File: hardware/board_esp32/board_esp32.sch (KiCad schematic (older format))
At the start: 91 parts

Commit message: removes MPPT IC and adds battery load switch
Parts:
- removed C?: 1uF, symbol Device:C_Small
- removed C? (x2): C_Small, symbol Device:C_Small
- removed D?: MBRS340, symbol Device:D_Schottky_Small
- removed D? (x2): STPS2L40U, symbol Device:D_Schottky_Small
- removed D? (x2): TPD1E10B06, Diode_SMD:D_0402_1005Metric, symbol Device:D_TVS
- removed J?: Conn_01x03, symbol Connector_Generic:Conn_01x03
- removed JP?: SolderJumper_2_Open, symbol Jumper:SolderJumper_2_Open
- removed L?: 22uH, symbol Device:L_Small
- removed R? (x4): 1K, symbol Device:R_Small
- removed R? (x2): NC, symbol Device:R_Small
- removed R? (x3): R_Small, symbol Device:R_Small
- removed R?: 0, symbol Device:R_Small
- removed TH?: NC, symbol Device:Thermistor_NTC
- removed U?: LT3652EMSE, Package_SO:MSOP-12-1EP_3x4mm_P0.65mm_EP1.65x2.85mm, symbol Battery_Management:LT3652EMSE
- added C?: 1nF, symbol Device:C_Small
- added J?: Micro_SD_Card_Det_Hirose_DM3AT, symbol Connector:Micro_SD_Card_Det_Hirose_DM3AT
- added J?: Conn_01x02, symbol Connector_Generic:Conn_01x02
- added JP? (x3): SolderJumper_2_Bridged, symbol Jumper:SolderJumper_2_Bridged
- added Q? (x2): AO3401, symbol Device:Q_PMOS_GDS
- added Q?: AO3400, symbol Device:Q_NMOS_GDS
- added R? (x2): 1K, symbol Device:R_Small
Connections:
- net labels removed: ~CHRG, ~FAULT
- wire segments 302 -> 248
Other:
- note added: "BATTERY INPUT 0-17V"
- note added: "BATTERY POWERS WHEN USB NOT CONNECTED"

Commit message: updates pin routing on ESP32
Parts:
- removed C?: 1nF, symbol Device:C_Small
- removed R? (x2): NC, symbol Device:R_Small
- removed R?: 10K, symbol Device:R_Small
- removed SW?: SW_Push, symbol symbols:SW_Push
- removed U?: FT230XS, Package_SO:SSOP-16_3.9x4.9mm_P0.635mm, symbol symbols:FT230XS
- added C? (x2): NC, symbol Device:C_Small
- added D?: BLUE, symbol Device:LED_Small
- added JP? (x15): SolderJumper_2_Bridged, symbol Jumper:SolderJumper_2_Bridged
- added R?: 10K, symbol Device:R_Small
- added U?: FT231XS, Package_SO:SSOP-20_3.9x8.7mm_P0.635mm, symbol symbols:FT231XS
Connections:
- net labels added: ESP_LED, FT_DCD, FT_DSR, FT_DTR, FT_RI, SD_CLK, SD_CMD, SD_DAT0, SD_DAT1, SD_DAT2, SD_DAT3, SD_DET_A, SD_DET_B
- net labels removed: LED0, LED1, SW_INPUT
- wire segments 248 -> 279
- no-connect marks 11 -> 8
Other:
- moved on the sheet: C?, D?, J?, JP?, R?, TP?

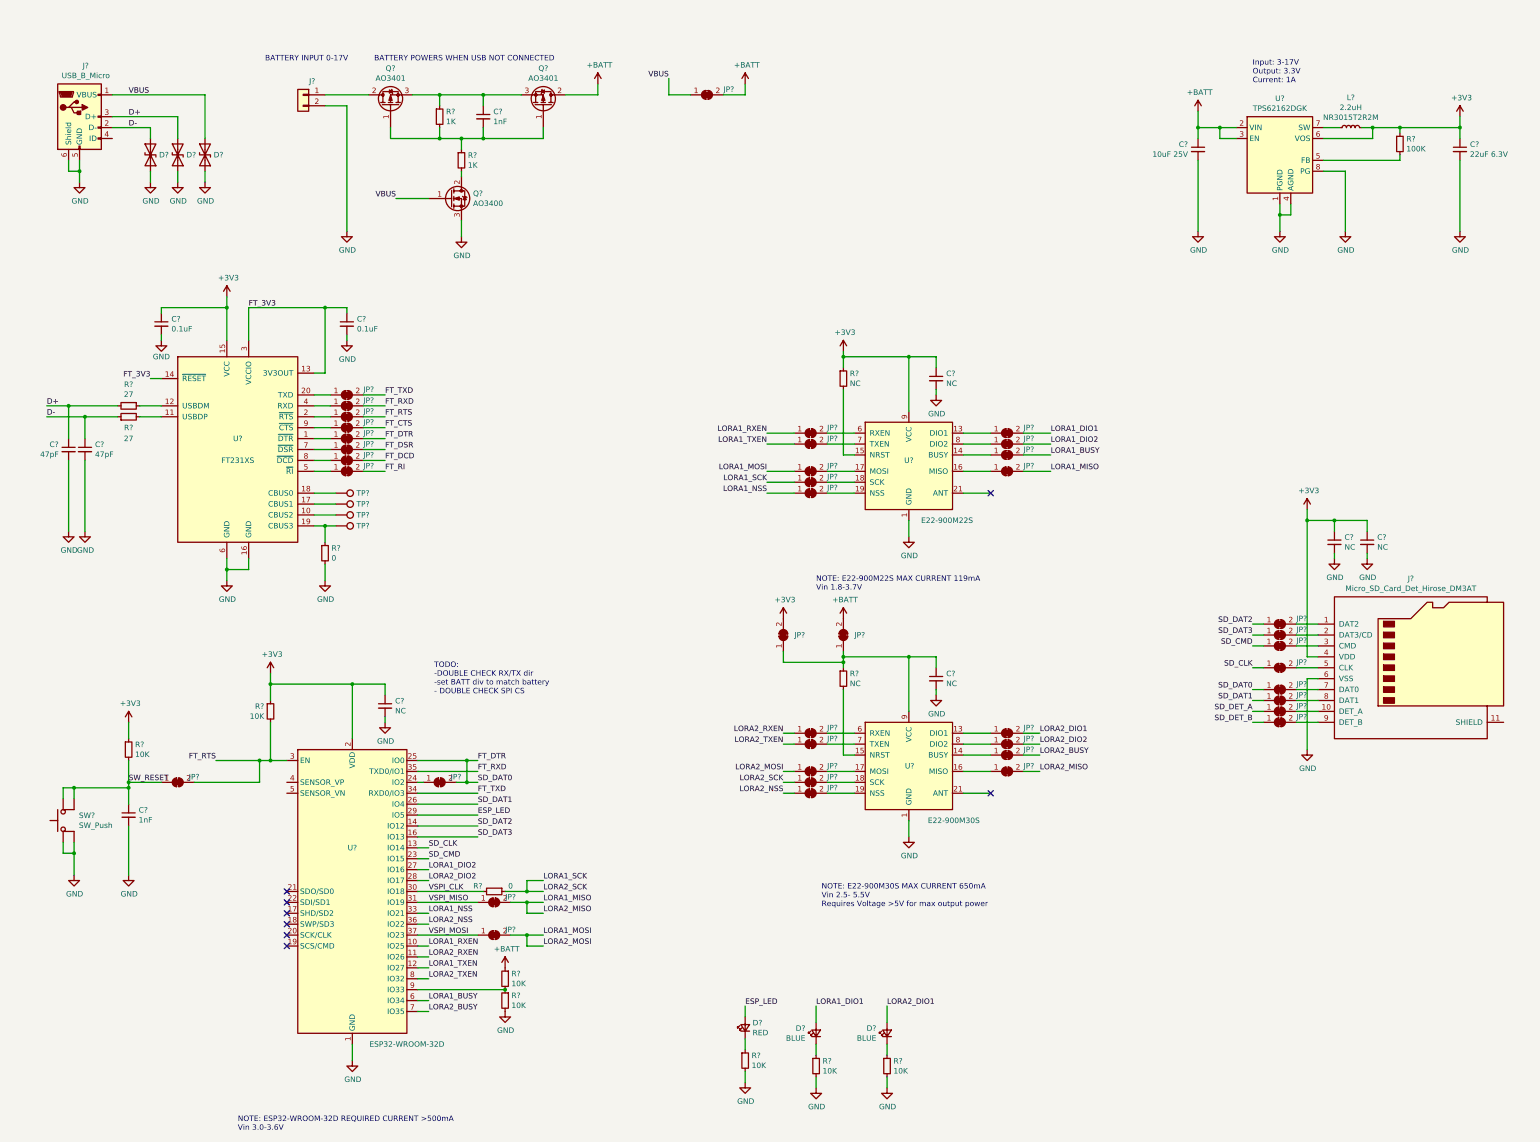
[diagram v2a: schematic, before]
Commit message: adds all footprints and starts work on routing out board ESP32
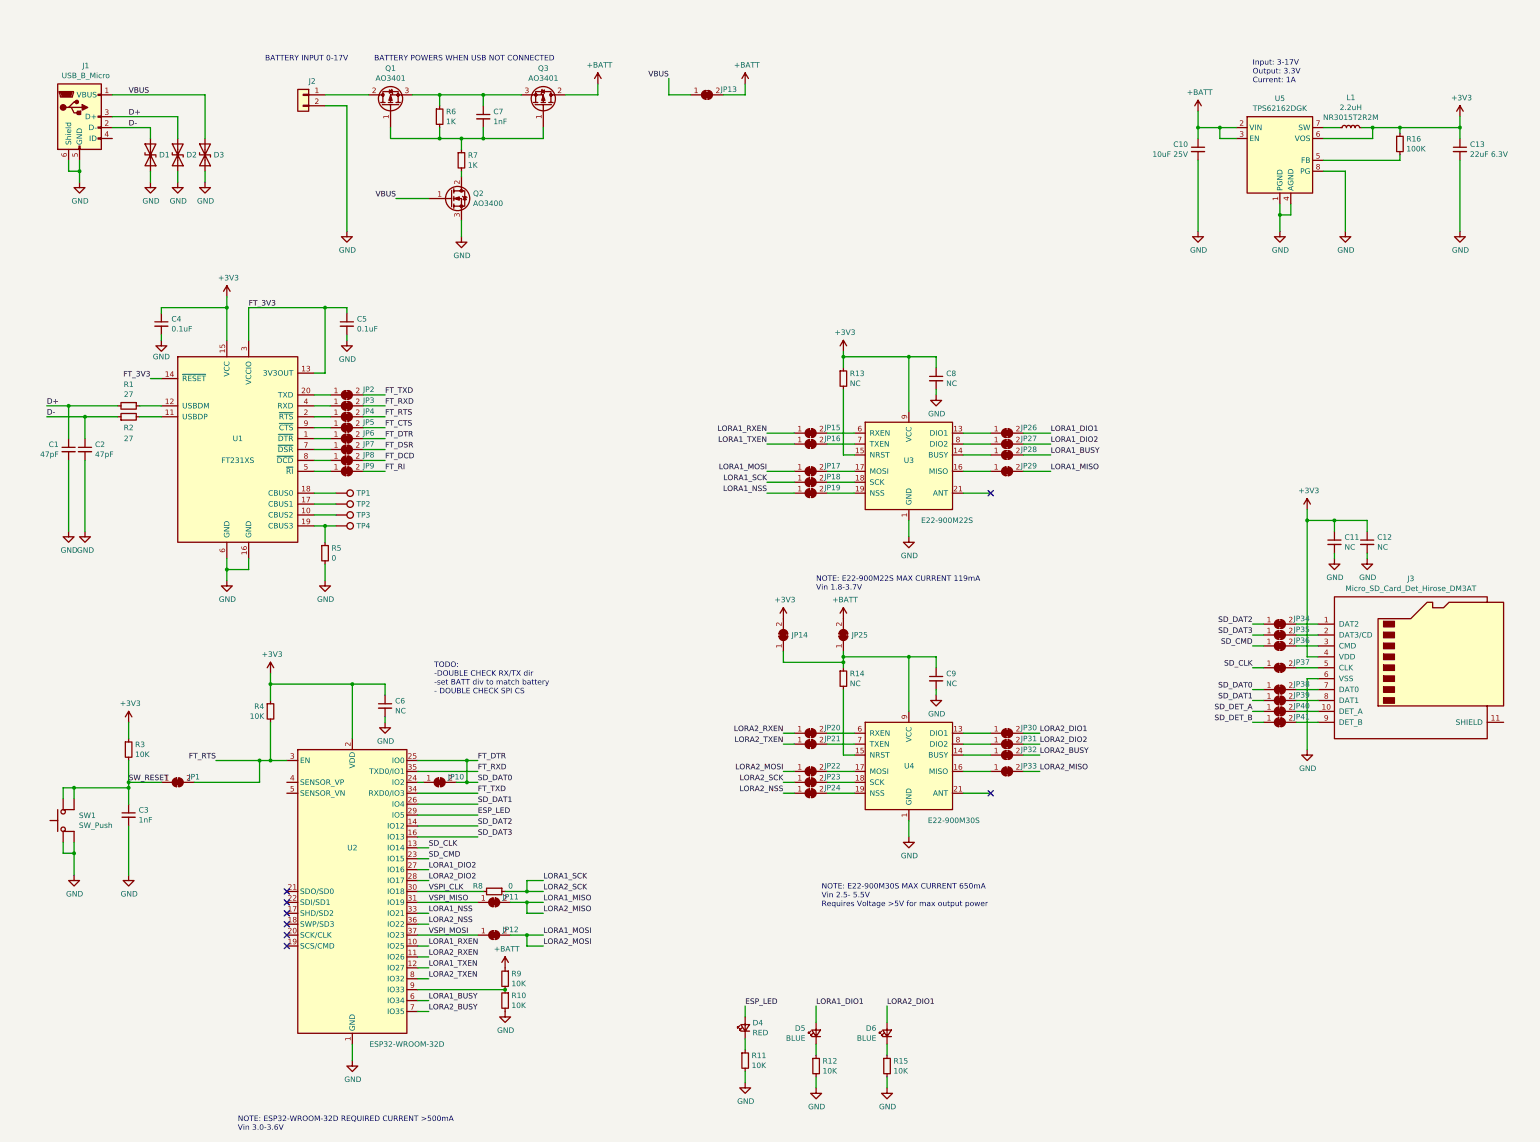
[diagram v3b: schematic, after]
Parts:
- C1, C12, C2, C3, C4, C5, C6, C7, C8, C9: renamed from C?; footprint (none) -> Capacitor_SMD:C_0402_1005Metric
- C10, C11, C13: renamed from C?; footprint (none) -> Capacitor_SMD:C_0805_2012Metric
- D4, D5, D6: renamed from D?; footprint (none) -> LED_SMD:LED_0603_1608Metric
- J1: renamed from J?; footprint (none) -> Connector_USB:USB_Micro-B_GCT_USB3076-30-A
- J2: renamed from J?; footprint (none) -> Connector_PinHeader_2.54mm:PinHeader_1x02_P2.54mm_Vertical
- J3: renamed from J?; footprint (none) -> Connector_Card:microSD_HC_Hirose_DM3D-SF
- JP1, JP10, JP11, JP12, JP13, JP14, JP15, JP16, JP17, JP18, JP19, JP2, JP20, JP21, JP22, JP23, JP24, JP25, JP26, JP27, JP28, JP29, JP3, JP30, JP31, JP32, JP33, JP34, JP35, JP36, JP37, JP38, JP39, JP4, JP40, JP41, JP5, JP6, JP7, JP8, JP9: renamed from JP?; footprint (none) -> Jumper:SolderJumper-2_P1.3mm_Bridged_RoundedPad1.0x1.5mm
- L1: renamed from L?; footprint (none) -> Inductor_SMD:L_Taiyo-Yuden_NR-30xx_HandSoldering
- Q1, Q2, Q3: renamed from Q?; footprint (none) -> Package_TO_SOT_SMD:SOT-23
- R1, R10, R11, R12, R13, R14, R15, R16, R2, R3, R4, R5, R6, R7, R8, R9: renamed from R?; footprint (none) -> Resistor_SMD:R_0402_1005Metric
- SW1: renamed from SW?; footprint (none) -> Button_Switch_SMD:SW_Push_1P1T-SH_NO_CK_KMR2xxG
- TP1, TP2, TP3, TP4: renamed from TP?; footprint (none) -> TestPoint:TestPoint_Pad_1.5x1.5mm
- U3: renamed from U?; footprint (none) -> parts:E22_900T22S
- U4: renamed from U?; footprint (none) -> parts:E22-900M30S
- gave numbers to parts that had none: 6

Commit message: adds changelog and pcb components are organised
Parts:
- removed C11: NC, Capacitor_SMD:C_0805_2012Metric, symbol Device:C_Small
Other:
- note added: "90 Ohm Diff Impedance"
- moved on the sheet: C12
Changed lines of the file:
@@
-	0    -1   -1   0
-$EndComp
-$Comp
-L Jumper:SolderJumper_2_Bridged JP14
-U 1 1 5DD3DBB8
-P 7700 6000
-F 0 "JP14" V 7700 5850 50  0000 C CNN
-F 1 "SolderJumper_2_Bridged" H 7700 6114 50  0001 C CNN
-F 2 "Jumper:SolderJumper-2_P1.3mm_Bridged_RoundedPad1.0x1.5mm" H 7700 6000 50  0001 C CNN
-F 3 "~" H 7700 6000 50  0001 C CNN
-	1    7700 6000
 	0    -1   -1   0
 $EndComp
@@
 $EndComp
 $Comp
-L Device:C_Small C11
-U 1 1 5DD91FE7
-P 12750 5150
-F 0 "C11" H 12842 5196 50  0000 L CNN
-F 1 "NC" H 12842 5105 50  0000 L CNN
-F 2 "Capacitor_SMD:C_0805_2012Metric" H 12750 5150 50  0001 C CNN
-F 3 "~" H 12750 5150 50  0001 C CNN
-	1    12750 5150
-	1    0    0    -1
-$EndComp
-$Comp
 L Device:C_Small C12
 U 1 1 5DD9356A
-P 13050 5150
-F 0 "C12" H 13142 5196 50  0000 L CNN
-F 1 "NC" H 13142 5105 50  0000 L CNN
-F 2 "Capacitor_SMD:C_0402_1005Metric" H 13050 5150 50  0001 C CNN
-F 3 "~" H 13050 5150 50  0001 C CNN
-	1    13050 5150
-	1    0    0    -1
-$EndComp
-$Comp
-L power:GND #PWR0140
-U 1 1 5DD93A75
-P 12750 5300
-F 0 "#PWR0140" H 12750 5050 50  0001 C CNN
-F 1 "GND" H 12755 5127 50  0000 C CNN
-F 2 "" H 12750 5300 50  0001 C CNN
-F 3 "" H 12750 5300 50  0001 C CNN
-	1    12750 5300
+P 12800 5150
+F 0 "C12" H 12892 5196 50  0000 L CNN
+F 1 "NC" H 12892 5105 50  0000 L CNN
+F 2 "Capacitor_SMD:C_0402_1005Metric" H 12800 5150 50  0001 C CNN
+F 3 "~" H 12800 5150 50  0001 C CNN
+	1    12800 5150
 	1    0    0    -1
 $EndComp
@@
 L power:GND #PWR0141
 U 1 1 5DD94190
-P 13050 5300
-F 0 "#PWR0141" H 13050 5050 50  0001 C CNN
-F 1 "GND" H 13055 5127 50  0000 C CNN
-F 2 "" H 13050 5300 50  0001 C CNN
-F 3 "" H 13050 5300 50  0001 C CNN
-	1    13050 5300
-	1    0    0    -1
-$EndComp
-Wire Wire Line
-	12500 4950 12750 4950
-Wire Wire Line
-	13050 4950 13050 5050
+P 12800 5300
+F 0 "#PWR0141" H 12800 5050 50  0001 C CNN
+F 1 "GND" H 12805 5127 50  0000 C CNN
+F 2 "" H 12800 5300 50  0001 C CNN
+F 3 "" H 12800 5300 50  0001 C CNN
+	1    12800 5300
+	1    0    0    -1
+$EndComp
+Wire Wire Line
+	12800 4950 12800 5050
 Connection ~ 12500 4950
 Wire Wire Line
 	12500 4950 12500 4850
 Wire Wire Line
-	12750 5050 12750 4950
-Connection ~ 12750 4950
-Wire Wire Line
-	12750 4950 13050 4950
-Wire Wire Line
-	12750 5250 12750 5300
-Wire Wire Line
-	13050 5300 13050 5250
+	12800 5300 12800 5250
 Wire Wire Line
 	12600 6400 12500 6400
@@
 	1    0    0    -1
 $EndComp
+$Comp
+L Jumper:SolderJumper_2_Bridged JP14
+U 1 1 5DD3DBB8
+P 7700 6000
+F 0 "JP14" V 7700 5850 50  0000 C CNN
+F 1 "SolderJumper_2_Bridged" H 7700 6114 50  0001 C CNN
+F 2 "Jumper:SolderJumper-2_P1.3mm_Bridged_RoundedPad1.0x1.5mm" H 7700 6000 50  0001 C CNN
+F 3 "~" H 7700 6000 50  0001 C CNN
+	1    7700 6000
+	0    -1   -1   0
+$EndComp
+Wire Wire Line
+	12500 4950 12800 4950
+Text Notes 600  3750 0    50   ~ 0
+90 Ohm Diff Impedance
 $EndSCHEMATC

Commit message: finishes placement and starts routing
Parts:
- added H1, H2, H3, H4: MountingHole_Pad, MountingHole:MountingHole_2.2mm_M2, symbol Mechanical:MountingHole_Pad
- SW1: symbol symbols:SW_Push -> board_esp32-rescue:SW_Push-symbols
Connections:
- net GND: now also H1.1, H2.1, H3.1, H4.1
- net LORA1_BUSY: now also U2.36 (IO22); no longer U2.6 (IO34)
- net LORA1_DIO2: now also U2.33 (IO21); no longer U2.27 (IO16)
- net LORA1_NSS: now also U2.27 (IO16); no longer U2.33 (IO21)
- net LORA1_RXEN: now also U2.12 (IO27); no longer U2.10 (IO25)
- net LORA1_TXEN: now also U2.10 (IO25); no longer U2.12 (IO27)
- net LORA2_NSS: now also U2.6 (IO34); no longer U2.36 (IO22)
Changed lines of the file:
@@
 Text Label 5500 8250 0    50   ~ 0
 LORA1_SCK
-Text Label 4450 8650 0    50   ~ 0
-LORA2_NSS
 Wire Wire Line
 	4350 8650 4450 8650
 Wire Wire Line
 	4350 8550 4450 8550
-Text Label 4450 8550 0    50   ~ 0
+Text Label 4450 8150 0    50   ~ 0
 LORA1_NSS
 Text Label 4450 8350 0    50   ~ 0
@@
 	1700 7550 1700 7400
 $Comp
-L symbols:SW_Push SW1
+L board_esp32-rescue:SW_Push-symbols SW1
 U 1 1 5DCB83D3
 P 1100 7700
@@
 Wire Wire Line
 	7350 10100 7350 10000
+Text Label 4450 9050 0    50   ~ 0
+LORA1_RXEN
 Text Label 4450 8850 0    50   ~ 0
-LORA1_RXEN
-Text Label 4450 9050 0    50   ~ 0
 LORA1_TXEN
 Wire Wire Line
@@
 Text Label 8000 9400 0    50   ~ 0
 LORA1_DIO1
-Text Label 4450 8150 0    50   ~ 0
+Text Label 4450 8550 0    50   ~ 0
 LORA1_DIO2
-Text Label 4450 9350 0    50   ~ 0
+Text Label 4450 8650 0    50   ~ 0
 LORA1_BUSY
 Text Label 4450 9450 0    50   ~ 0
@@
 Wire Wire Line
 	4450 8250 4350 8250
-Text Label 4450 8250 0    50   ~ 0
-LORA2_DIO2
 Text Label 4450 8950 0    50   ~ 0
 LORA2_RXEN
@@
 Text Notes 600  3750 0    50   ~ 0
 90 Ohm Diff Impedance
+$Comp
+L Mechanical:MountingHole_Pad H1
+U 1 1 5DF9D839
+P 11200 8450
+F 0 "H1" H 11300 8453 50  0000 L CNN
+F 1 "MountingHole_Pad" H 11300 8408 50  0001 L CNN
+F 2 "MountingHole:MountingHole_2.2mm_M2" H 11200 8450 50  0001 C CNN
+F 3 "~" H 11200 8450 50  0001 C CNN
+	1    11200 8450
+	1    0    0    -1
+$EndComp
+Wire Wire Line
+	11200 8550 11200 8650
+$Comp
+L power:GND #PWR0140
+U 1 1 5DFA02C2
+P 11200 8650
+F 0 "#PWR0140" H 11200 8400 50  0001 C CNN
+F 1 "GND" H 11205 8477 50  0000 C CNN
+F 2 "" H 11200 8650 50  0001 C CNN
+F 3 "" H 11200 8650 50  0001 C CNN
+	1    11200 8650
+	1    0    0    -1
+$EndComp
+$Comp
+L power:GND #PWR0144
+U 1 1 5DFA0824
+P 11500 8650
+F 0 "#PWR0144" H 11500 8400 50  0001 C CNN
+F 1 "GND" H 11505 8477 50  0000 C CNN
+F 2 "" H 11500 8650 50  0001 C CNN
+F 3 "" H 11500 8650 50  0001 C CNN
+	1    11500 8650
+	1    0    0    -1
+$EndComp
+Wire Wire Line
+	11500 8550 11500 8650
+$Comp
+L Mechanical:MountingHole_Pad H2
+U 1 1 5DFA0832
+P 11500 8450
+F 0 "H2" H 11600 8453 50  0000 L CNN
+F 1 "MountingHole_Pad" H 11600 8408 50  0001 L CNN
+F 2 "MountingHole:MountingHole_2.2mm_M2" H 11500 8450 50  0001 C CNN
+F 3 "~" H 11500 8450 50  0001 C CNN
+	1    11500 8450
+	1    0    0    -1
+$EndComp
+$Comp
+L power:GND #PWR0145
+U 1 1 5DFA0EBF
+P 11800 8650
+F 0 "#PWR0145" H 11800 8400 50  0001 C CNN
+F 1 "GND" H 11805 8477 50  0000 C CNN
+F 2 "" H 11800 8650 50  0001 C CNN
+F 3 "" H 11800 8650 50  0001 C CNN
+	1    11800 8650
+	1    0    0    -1
+$EndComp
+Wire Wire Line
+	11800 8550 11800 8650
+$Comp
+L Mechanical:MountingHole_Pad H3
+U 1 1 5DFA0ECD
+P 11800 8450
+F 0 "H3" H 11900 8453 50  0000 L CNN
+F 1 "MountingHole_Pad" H 11900 8408 50  0001 L CNN
+F 2 "MountingHole:MountingHole_2.2mm_M2" H 11800 8450 50  0001 C CNN
+F 3 "~" H 11800 8450 50  0001 C CNN
+	1    11800 8450
+	1    0    0    -1
+$EndComp
+Wire Wire Line
+	12100 8550 12100 8650
+$Comp
+L power:GND #PWR0146
+U 1 1 5DFA14BF
+P 12100 8650
+F 0 "#PWR0146" H 12100 8400 50  0001 C CNN
+F 1 "GND" H 12105 8477 50  0000 C CNN
+F 2 "" H 12100 8650 50  0001 C CNN
+F 3 "" H 12100 8650 50  0001 C CNN
+	1    12100 8650
+	1    0    0    -1
+$EndComp
+$Comp
+L Mechanical:MountingHole_Pad H4
+U 1 1 5DFA14CC
+P 12100 8450
+F 0 "H4" H 12200 8453 50  0000 L CNN
+F 1 "MountingHole_Pad" H 12200 8408 50  0001 L CNN
+F 2 "MountingHole:MountingHole_2.2mm_M2" H 12100 8450 50  0001 C CNN
+F 3 "~" H 12100 8450 50  0001 C CNN
+	1    12100 8450
+	1    0    0    -1
+$EndComp
+Text Label 4450 9350 0    50   ~ 0
+LORA2_NSS
+Text Label 4450 8250 0    50   ~ 0
+LORA2_DIO2
 $EndSCHEMATC
